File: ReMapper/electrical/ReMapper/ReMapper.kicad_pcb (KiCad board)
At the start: 4 copper layers, 95.8 x 48.2 mm, 51 parts, among them J2 USB_IN, J5 USB_OUT, U1 ESP32-S3-WROOM-1-N8R8, U2 RP2040, U3 W25Q128JVE, U4 RT6150B-33GQW, U5 W25Q128JVE, Y1 12MHZ

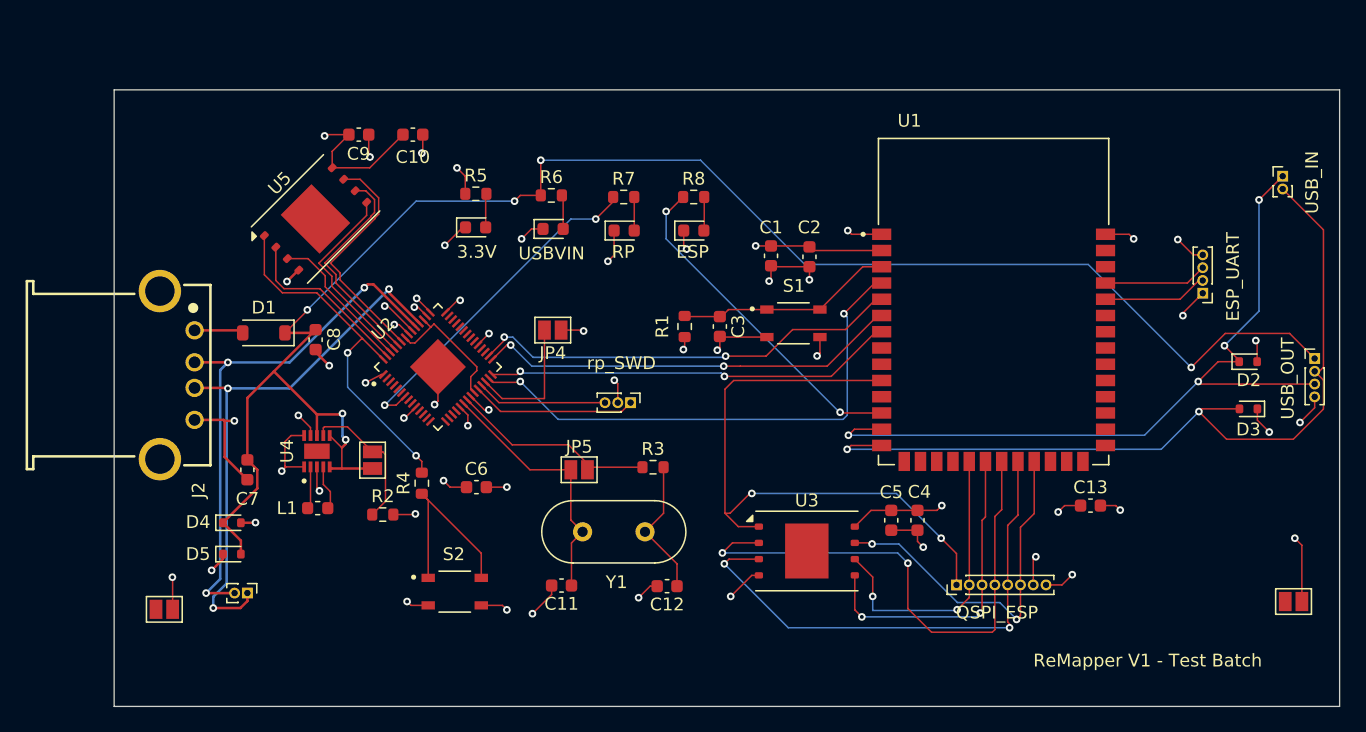
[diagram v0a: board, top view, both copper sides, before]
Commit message: picked basic parts from lcsc, pre fab
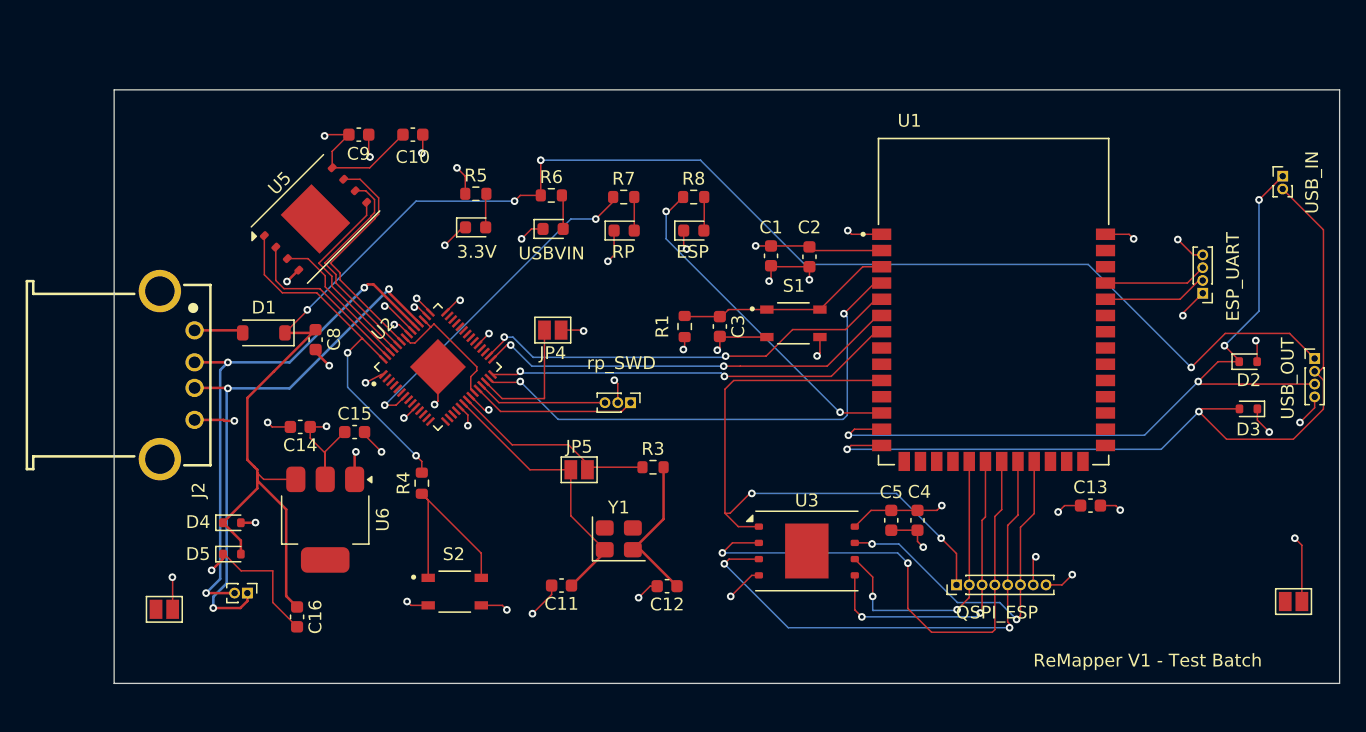
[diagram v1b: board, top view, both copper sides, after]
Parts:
- removed C6, C7: 47uF, Capacitor_SMD:C_0603_1608Metric
- removed JP1: PFM Mode, Jumper:SolderJumper-2_P1.3mm_Open_Pad1.0x1.5mm
- removed L1: 2.2uH, Inductor_SMD:L_0603_1608Metric
- removed R2: 100k, Resistor_SMD:R_0603_1608Metric
- removed U4: RT6150B-33GQW, footprints:RT6150B-33GQW
- added C14: 47uF, Capacitor_SMD:C_0603_1608Metric, F.Cu at (103.5, 103.8)
- added C15: 0.1uf, Capacitor_SMD:C_0603_1608Metric, F.Cu at (107.7, 104.2)
- added C16: 47uF, Capacitor_SMD:C_0603_1608Metric, F.Cu at (103.2, 118.7)
- added U6: SPX1117M3-L-3-3/TR, Package_TO_SOT_SMD:SOT-223, F.Cu at (105.4, 111.1)
- Y1: footprint Crystal:Crystal_HC49-4H_Vertical -> Crystal:Crystal_SMD_3225-4Pin_3.2x2.5mm
- moved Y1 2.88 mm to (128.3, 112.6)
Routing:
- net Net-(JP1-A): track 11.5 -> 0.00 mm
- net Net-(U4-LX1): track 3.54 -> 0.00 mm
- net Net-(U4-LX2): track 3.32 -> 0.00 mm
- net GND: track 92.2 -> 95.4 mm, vias 38 -> 37
- net /USB_VIN: track 138.3 -> 135.6 mm, vias 6 -> 4
- net /3.3V: track 63.2 -> 65.7 mm, vias 20 -> 19
- net /XIN_rp: track 20.3 -> 21.8 mm
- net Net-(C12-Pad1): track 10.9 -> 12.1 mm
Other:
- board size 95.8 x 48.2 mm -> 95.8 x 46.4 mm

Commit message: fixed up V1, added some debug. Now working on V2
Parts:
- removed Y1: 12MHZ, Crystal:Crystal_SMD_3225-4Pin_3.2x2.5mm
- added JP1: VIN_Schottky, Jumper:SolderJumper-2_P1.3mm_Open_Pad1.0x1.5mm, F.Cu at (138.3, 101.0)
- added S3: SKRPABE010, footprints:push_button_SKRPABE010, F.Cu at (118.9, 116.3)
- added Y2: 12MHZ, Crystal:Crystal_SMD_3225-4Pin_3.2x2.5mm, F.Cu at (143.4, 95.0)
- ESP_QSPI1: footprint Connector_PinHeader_1.00mm:PinHeader_1x08_P1.00mm_Vertical -> Connector_PinHeader_2.54mm:PinHeader_1x08_P2.54mm_Vertical
- ESP_UART0: footprint Connector_PinHeader_1.00mm:PinHeader_1x04_P1.00mm_Vertical -> Connector_PinHeader_2.54mm:PinHeader_1x04_P2.54mm_Vertical
- RP_SWD1: footprint Connector_PinHeader_1.00mm:PinHeader_1x03_P1.00mm_Vertical -> Connector_PinHeader_2.54mm:PinHeader_1x03_P2.54mm_Vertical
- USB_IN1, USB_OUT1: footprint Connector_PinHeader_1.00mm:PinHeader_1x02_P1.00mm_Vertical -> Connector_PinHeader_2.54mm:PinHeader_1x02_P2.54mm_Vertical
- moved J2 62.3 mm to (149.7, 84.8), turned to 0 degrees
- moved U5 57.9 mm to (157.8, 110.5), turned to 0 degrees
- moved J5 52.8 mm to (133.8, 118.1)
- moved ESP_UART0 51.2 mm to (124.6, 106.7), turned to 0 degrees
- moved C9 48.8 mm to (142.5, 115.5)
- moved USB_OUT1 47.9 mm to (147.4, 119.1)
- moved U2 47.8 mm to (157.7, 119.0), turned to 0 degrees
- moved JP2 47.5 mm to (138.3, 104.5)
- moved D2 45.3 mm to (132.7, 105.6)
- moved D3 45.2 mm to (132.7, 108.1), turned to 0 degrees
- moved JP3 43.8 mm to (138.3, 108.1)
- moved C14 43.6 mm to (146.5, 110.5), turned to 0 degrees
- moved USB_IN1 43.5 mm to (142.8, 119.1), turned to 0 degrees
- moved C16 43.4 mm to (146.5, 115.5), turned to 0 degrees
- moved C8 41.1 mm to (142.5, 113.0), turned to 0 degrees
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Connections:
- U1 pad 27: unconnected-(U1-IO0-Pad27) -> /ESP_IO0
- U2 pad 46: /USB_IN_D+ -> /USB_IN_D-
- U2 pad 47: /USB_IN_D- -> /USB_IN_D+
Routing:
- net /USB_VIN: track 135.6 -> 0.00 mm, vias 4 -> 0
- net GND: track 95.4 -> 0.00 mm, vias 37 -> 0
- net /3.3V: track 65.7 -> 0.00 mm, vias 19 -> 0
- net /USB_OUT_D-: track 65.7 -> 0.00 mm, vias 2 -> 0
- net /USB_OUT_D+: track 61.8 -> 0.00 mm, vias 4 -> 0
- net /QSPI_CS_esp: track 48.5 -> 0.00 mm, vias 2 -> 0
- net /USB_IN_D+: track 43.3 -> 0.00 mm, vias 3 -> 0
- net /QSPI_IO1_esp: track 42.6 -> 0.00 mm, vias 2 -> 0
- net /USB_IN_D-: track 42.2 -> 0.00 mm, vias 3 -> 0
- net /SPI2_MOSI: track 41.5 -> 0.00 mm, vias 2 -> 0
- net /QSPI_IO2_esp: track 40.6 -> 0.00 mm, vias 2 -> 0
- net /SPI2_MISO: track 34.0 -> 0.00 mm, vias 2 -> 0
- net /SPI2_CLK: track 33.2 -> 0.00 mm, vias 2 -> 0
- net /SPI2_CS: track 32.1 -> 0.00 mm, vias 2 -> 0
- net /QSPI_CS_rp: track 28.5 -> 0.00 mm, vias 2 -> 0
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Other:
- board outline removed
- board text removed: "3.3V"
- board text removed: "ESP"
- board text removed: "ESP_UART"
- board text removed: "QSPI_ESP"
- board text removed: "RP"
- board text removed: "ReMapper V1 - Test Batch"
- board text removed: "USBVIN"
- board text removed: "USB_IN"
- board text removed: "USB_OUT"
- board text removed: "rp_SWD"

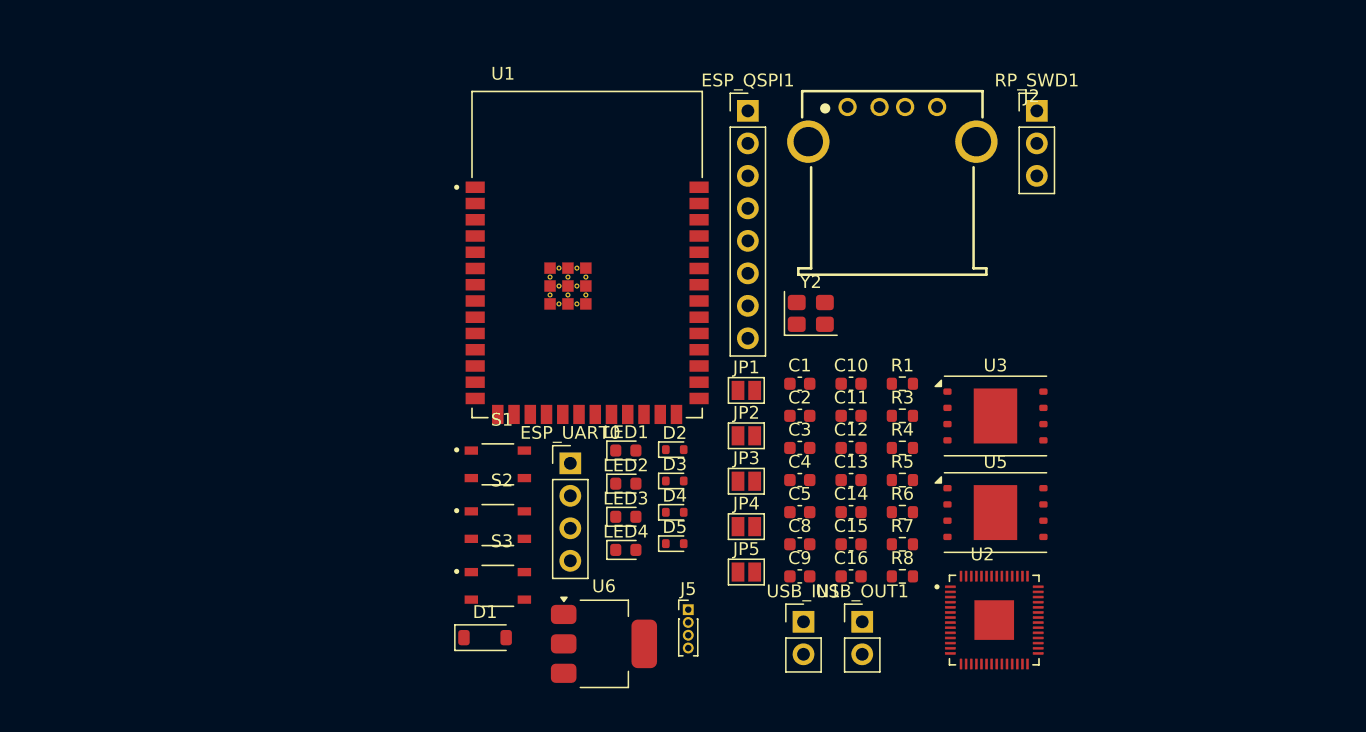
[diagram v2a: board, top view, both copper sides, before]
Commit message: Remapper started V2 Layout
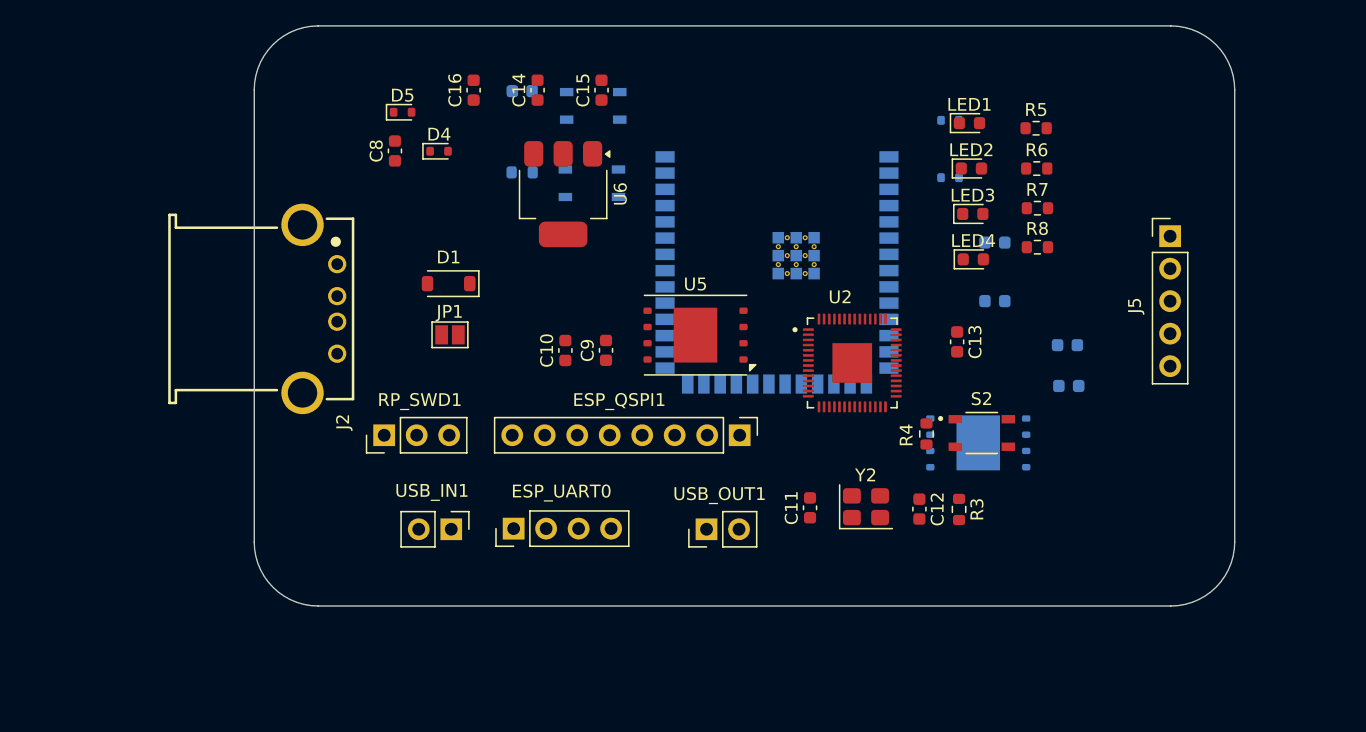
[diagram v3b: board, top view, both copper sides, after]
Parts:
- removed JP2, JP3: GND_SHIELD, Jumper:SolderJumper-2_P1.3mm_Open_Pad1.0x1.5mm
- removed JP4: RP_RUN, Jumper:SolderJumper-2_P1.3mm_Open_Pad1.0x1.5mm
- removed JP5: RP_crystal, Jumper:SolderJumper-2_P1.3mm_Open_Pad1.0x1.5mm
- C1, C2, C3, C4, C5, D2, D3, R1, S1, S3, U1, U3: moved to B.Cu
- J5: footprint Connector_PinHeader_1.00mm:PinHeader_1x04_P1.00mm_Vertical -> Connector_PinHeader_2.54mm:PinHeader_1x05_P2.54mm_Vertical
- moved RP_SWD1 57.0 mm to (110.0, 104.5), turned to 90 degrees
- moved J2 50.3 mm to (100.4, 94.6), turned to -90 degrees
- moved C16 48.1 mm to (117.0, 77.5), turned to 90 degrees
- moved J5 47.7 mm to (171.4, 88.9)
- moved C8 44.1 mm to (110.8, 82.3), turned to 90 degrees
- moved C14 41.1 mm to (122.0, 77.5), turned to 90 degrees
- moved C15 40.5 mm to (127.0, 77.5), turned to 90 degrees
- moved D5 39.9 mm to (111.5, 79.2)
- moved S2 38.5 mm to (156.7, 104.3)
- moved LED1 37.1 mm to (155.8, 80.1)
- moved LED2 36.6 mm to (155.9, 83.7)
- moved LED3 36.0 mm to (156.0, 87.2)
- moved LED4 35.4 mm to (156.1, 90.8)
- moved C3 35.3 mm to (120.8, 77.6), turned to 180 degrees
- moved U6 35.3 mm to (124.0, 85.7), turned to -90 degrees
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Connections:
- U2 pad 26: Net-(JP4-B) -> unconnected-(U2-RUN-Pad26)
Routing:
- removed copper zone on In2.Cu, net /3.3V
- removed copper zone on In1.Cu, net GND
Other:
- board outline added: 76.7 x 45.3 mm

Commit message: started routing... not looking good, might start again
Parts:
- C1, C2, C3, C4, C5, D2, D3, R1, S1, S3, U3: moved to F.Cu
- moved D5 18.2 mm to (129.6, 80.8), turned to 180 degrees
- moved R4 18.2 mm to (169.6, 110.3), turned to 0 degrees
- moved D3 16.5 mm to (170.7, 82.3)
- moved D2 16.4 mm to (170.7, 79.7), turned to 0 degrees
- moved S2 12.9 mm to (169.5, 106.0), turned to 90 degrees
- moved S1 11.1 mm to (135.7, 84.7), turned to 0 degrees
- moved S3 10.9 mm to (135.8, 89.9), turned to 0 degrees
- moved C5 9.93 mm to (153.6, 100.7), turned to 0 degrees
- moved C4 9.73 mm to (153.7, 97.5), turned to 0 degrees
- moved R1 9.62 mm to (111.5, 86.4)
- moved C3 9.55 mm to (111.5, 79.5), turned to 0 degrees
- moved C2 5.86 mm to (163.6, 93.8), turned to 0 degrees
- moved LED1 5.81 mm to (161.0, 77.6), turned to 180 degrees
- moved LED2 5.81 mm to (161.2, 81.2), turned to 180 degrees
- moved LED3 5.81 mm to (161.3, 84.7), turned to 180 degrees
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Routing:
- net GND: track 0.00 -> 134.7 mm, vias 0 -> 34
- net /USB_OUT_D+: track 0.00 -> 82.8 mm, vias 0 -> 2
- net /USB_OUT_D-: track 0.00 -> 67.1 mm, vias 0 -> 2
- net /3.3V: track 0.00 -> 60.3 mm, vias 0 -> 8
- net Net-(U1-EN): track 0.00 -> 45.6 mm
- net /USB_VIN: track 0.00 -> 44.7 mm, vias 0 -> 2
- net /ESP_TXDO: track 0.00 -> 28.4 mm, vias 0 -> 2
- net /ESP_RXDO: track 0.00 -> 28.2 mm
- net /QSPI_IO3_rp: track 0.00 -> 22.8 mm
- net /USB_IN_D-: track 0.00 -> 22.3 mm, vias 0 -> 1
- net /USB_IN_D+: track 0.00 -> 21.8 mm, vias 0 -> 1
- net /QSPI_CLK_rp: track 0.00 -> 20.2 mm
- net /XIN_rp: track 0.00 -> 17.6 mm, vias 0 -> 2
- net /QSPI_IO0_rp: track 0.00 -> 17.2 mm
- net /XOUT_rp: track 0.00 -> 12.5 mm
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- added copper zone on In2.Cu, net /3.3V
- added copper zone on In1.Cu, net GND

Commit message: trying to pass DRC
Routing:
- net /USB_VIN: track 44.7 -> 118.9 mm, vias 2 -> 3
- net /QSPI_IO3_esp: track 0.00 -> 69.4 mm, vias 0 -> 3
- net /QSPI_CLK_esp: track 0.00 -> 69.2 mm, vias 0 -> 3
- net /QSPI_IO0_esp: track 0.00 -> 69.0 mm, vias 0 -> 3
- net /USB_IN_D-: track 22.3 -> 85.3 mm, vias 1 -> 3
- net /SWDIO_rp: track 0.00 -> 61.0 mm, vias 0 -> 4
- net /QSPI_CS_rp: track 9.86 -> 68.2 mm
- net /SWCLK_rp: track 0.00 -> 55.7 mm, vias 0 -> 6
- net /QSPI_IO2_esp: track 0.00 -> 46.3 mm, vias 0 -> 2
- net /USB_IN_D+: track 21.8 -> 67.1 mm, vias 1 -> 2
- net /QSPI_IO1_esp: track 0.00 -> 37.8 mm, vias 0 -> 2
- net /QSPI_CS_esp: track 0.00 -> 35.2 mm, vias 0 -> 2
- net /GPIO5_rp: track 0.00 -> 34.1 mm, vias 0 -> 2
- net /SPI2_MOSI: track 0.00 -> 29.0 mm, vias 0 -> 3
- net /USB_OUT_D-: track 67.1 -> 90.6 mm, vias 2 -> 3
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
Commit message: V2 passing DRC
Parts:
- removed USB_OUT1: USB_OUT_Debug, Connector_PinHeader_2.54mm:PinHeader_1x02_P2.54mm_Vertical
- U1: footprint footprints:XCVR_ESP32S3WROOM1N8R8 -> RF_Module:ESP32-S3-WROOM-1
- moved C14 24.2 mm to (145.3, 84.2)
- moved C15 22.5 mm to (148.5, 84.2)
- moved RP_SWD1 21.2 mm to (129.4, 112.9)
- moved C4 9.24 mm to (147.3, 90.8)
- moved C1 6.84 mm to (162.7, 100.2)
- moved C2 6.84 mm to (166.3, 100.0)
- moved ESP_QSPI1 6.17 mm to (131.7, 105.4)
- moved LED1 5.99 mm to (163.7, 83.0)
- moved LED2 5.99 mm to (163.9, 86.5)
- moved R6 5.99 mm to (159.4, 88.2)
- moved R8 5.99 mm to (159.4, 94.4)
- moved LED3 5.99 mm to (164.0, 90.0)
- moved LED4 5.99 mm to (164.0, 93.6)
- moved R5 5.99 mm to (159.3, 85.1)
- moved R7 5.99 mm to (159.4, 91.3)
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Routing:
- net GND: track 138.7 -> 78.2 mm
- net /USB_OUT_D-: track 90.6 -> 36.6 mm, vias 3 -> 1
- net /USB_OUT_D+: track 82.8 -> 39.3 mm, vias 2 -> 1
- net /SWDIO_rp: track 61.0 -> 27.5 mm, vias 4 -> 2
- net /QSPI_CLK_esp: track 69.2 -> 37.5 mm, vias 3 -> 2
- net /QSPI_IO0_esp: track 69.0 -> 39.7 mm, vias 3 -> 1
- net /USB_VIN: track 118.9 -> 90.8 mm, vias 3 -> 0
- net /USB_IN_D-: track 85.3 -> 60.5 mm, vias 3 -> 2
- net /3.3V: track 73.9 -> 49.8 mm, vias 14 -> 21
- net /QSPI_CS_esp: track 35.2 -> 57.8 mm
- net /SWCLK_rp: track 55.7 -> 34.1 mm, vias 6 -> 2
- net /QSPI_IO3_esp: track 69.4 -> 49.1 mm, vias 3 -> 1
- net /QSPI_IO3_rp: track 22.8 -> 7.24 mm
- net /QSPI_IO1_esp: track 37.8 -> 53.2 mm
- net /QSPI_CLK_rp: track 20.2 -> 5.80 mm
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
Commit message: added some silkscreen, sent V2 ReMapper to FAB
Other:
- outline, holes or cut-outs redrawn
- board text added: "3.3V"
- board text added: "CLK"
- board text added: "D+"
- board text added: "D-"
- board text added: "DreamingDoveLabs"
- board text added: "ESP EN"
- board text added: "ESP IO0"
- board text added: "ESP IO8"
- board text added: "GND"
- board text added: "IO"
- board text added: "PWR Passthrough"
- board text added: "RP GPIO5"
- board text added: "RP RESET"
- board text added: "RX"
- board text added: "ReMapper V2"
- board text added: "TX"
- board text added: "USB VIN"
- board text added: "USB Vin"
- board text added: "VIN"
